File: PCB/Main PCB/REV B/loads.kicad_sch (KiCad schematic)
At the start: 13 parts, among them J10 Ignitor, J11 Auger, J12 FAN, K1 CPC1966Y, U7 AQH3223A, U8 AQH3223A

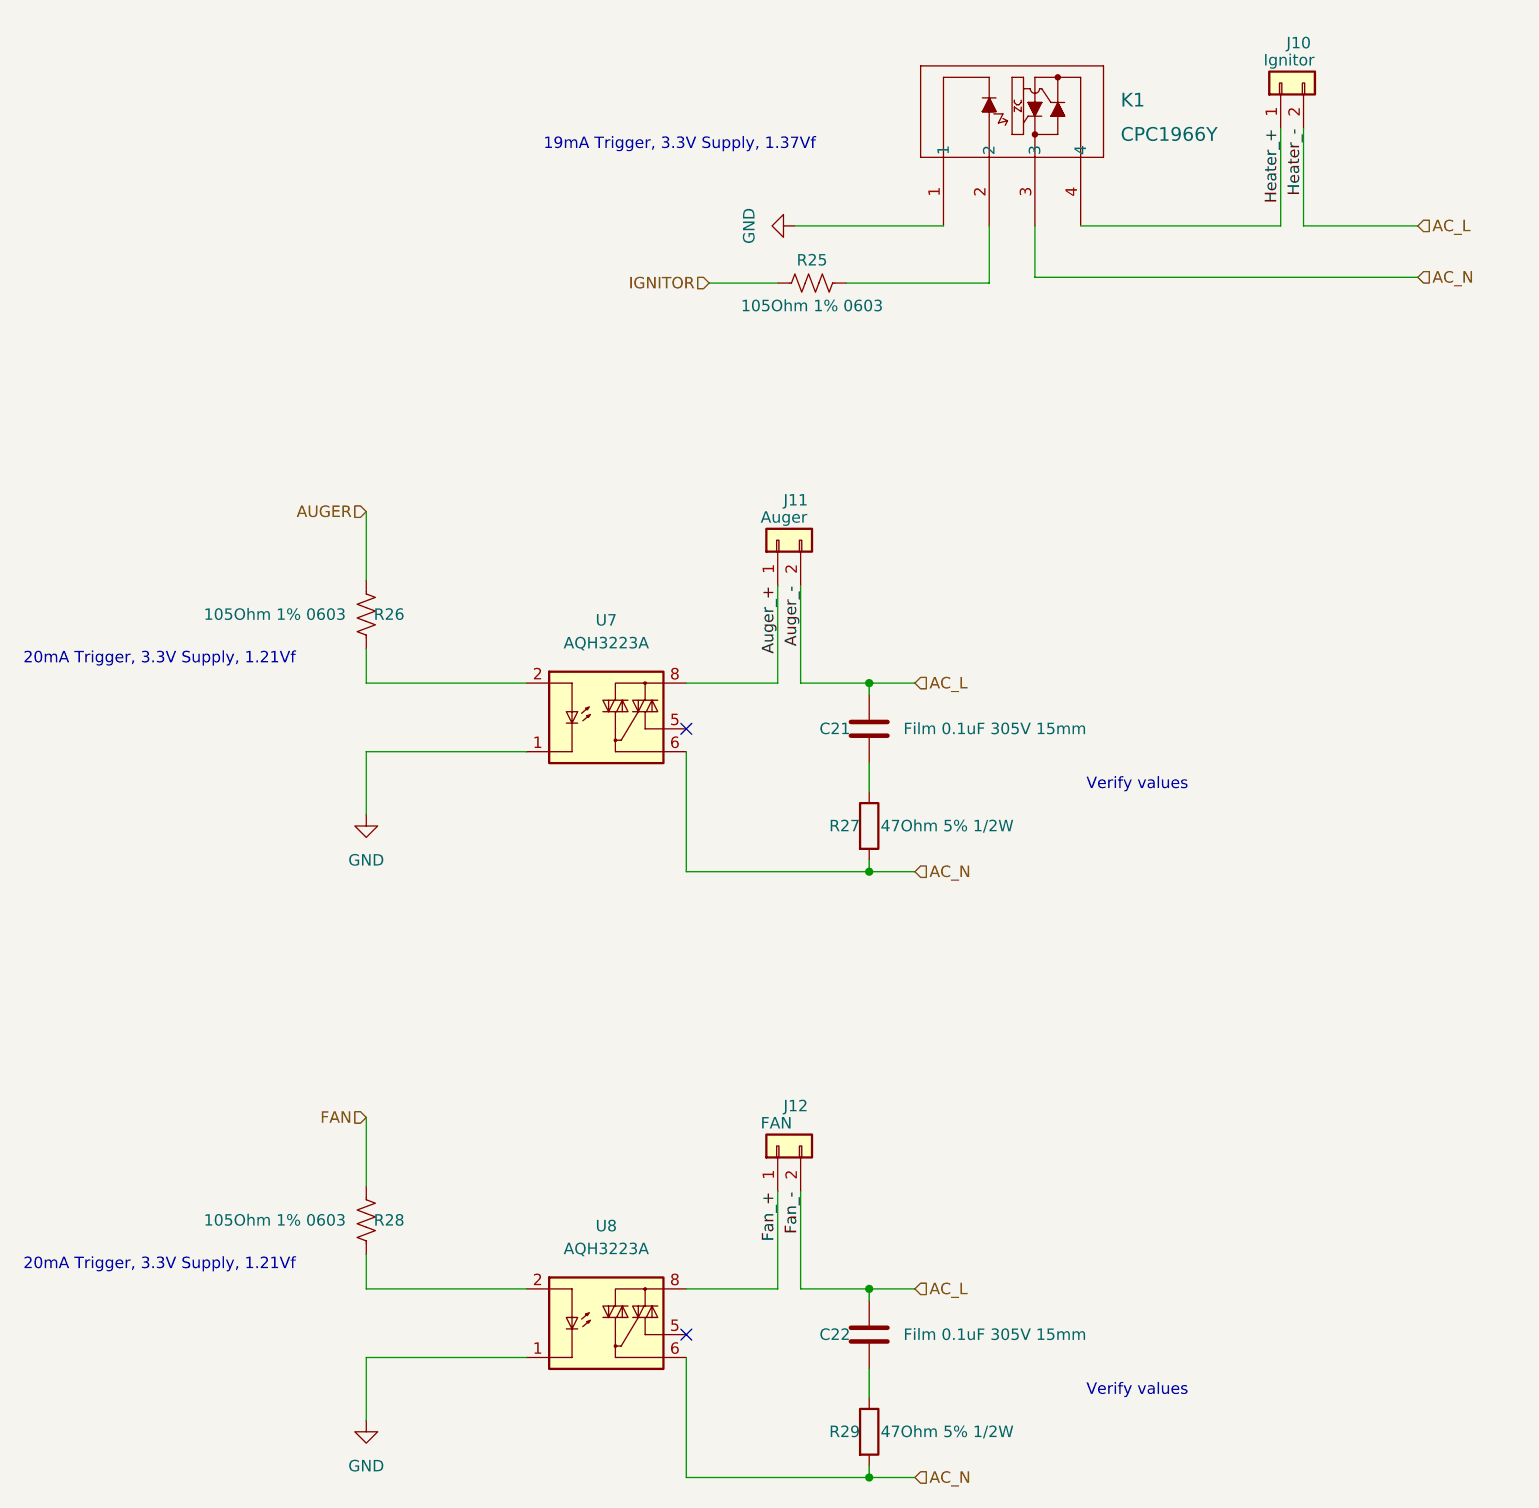
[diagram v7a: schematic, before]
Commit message: PCB schematic updates, added 5V power supply
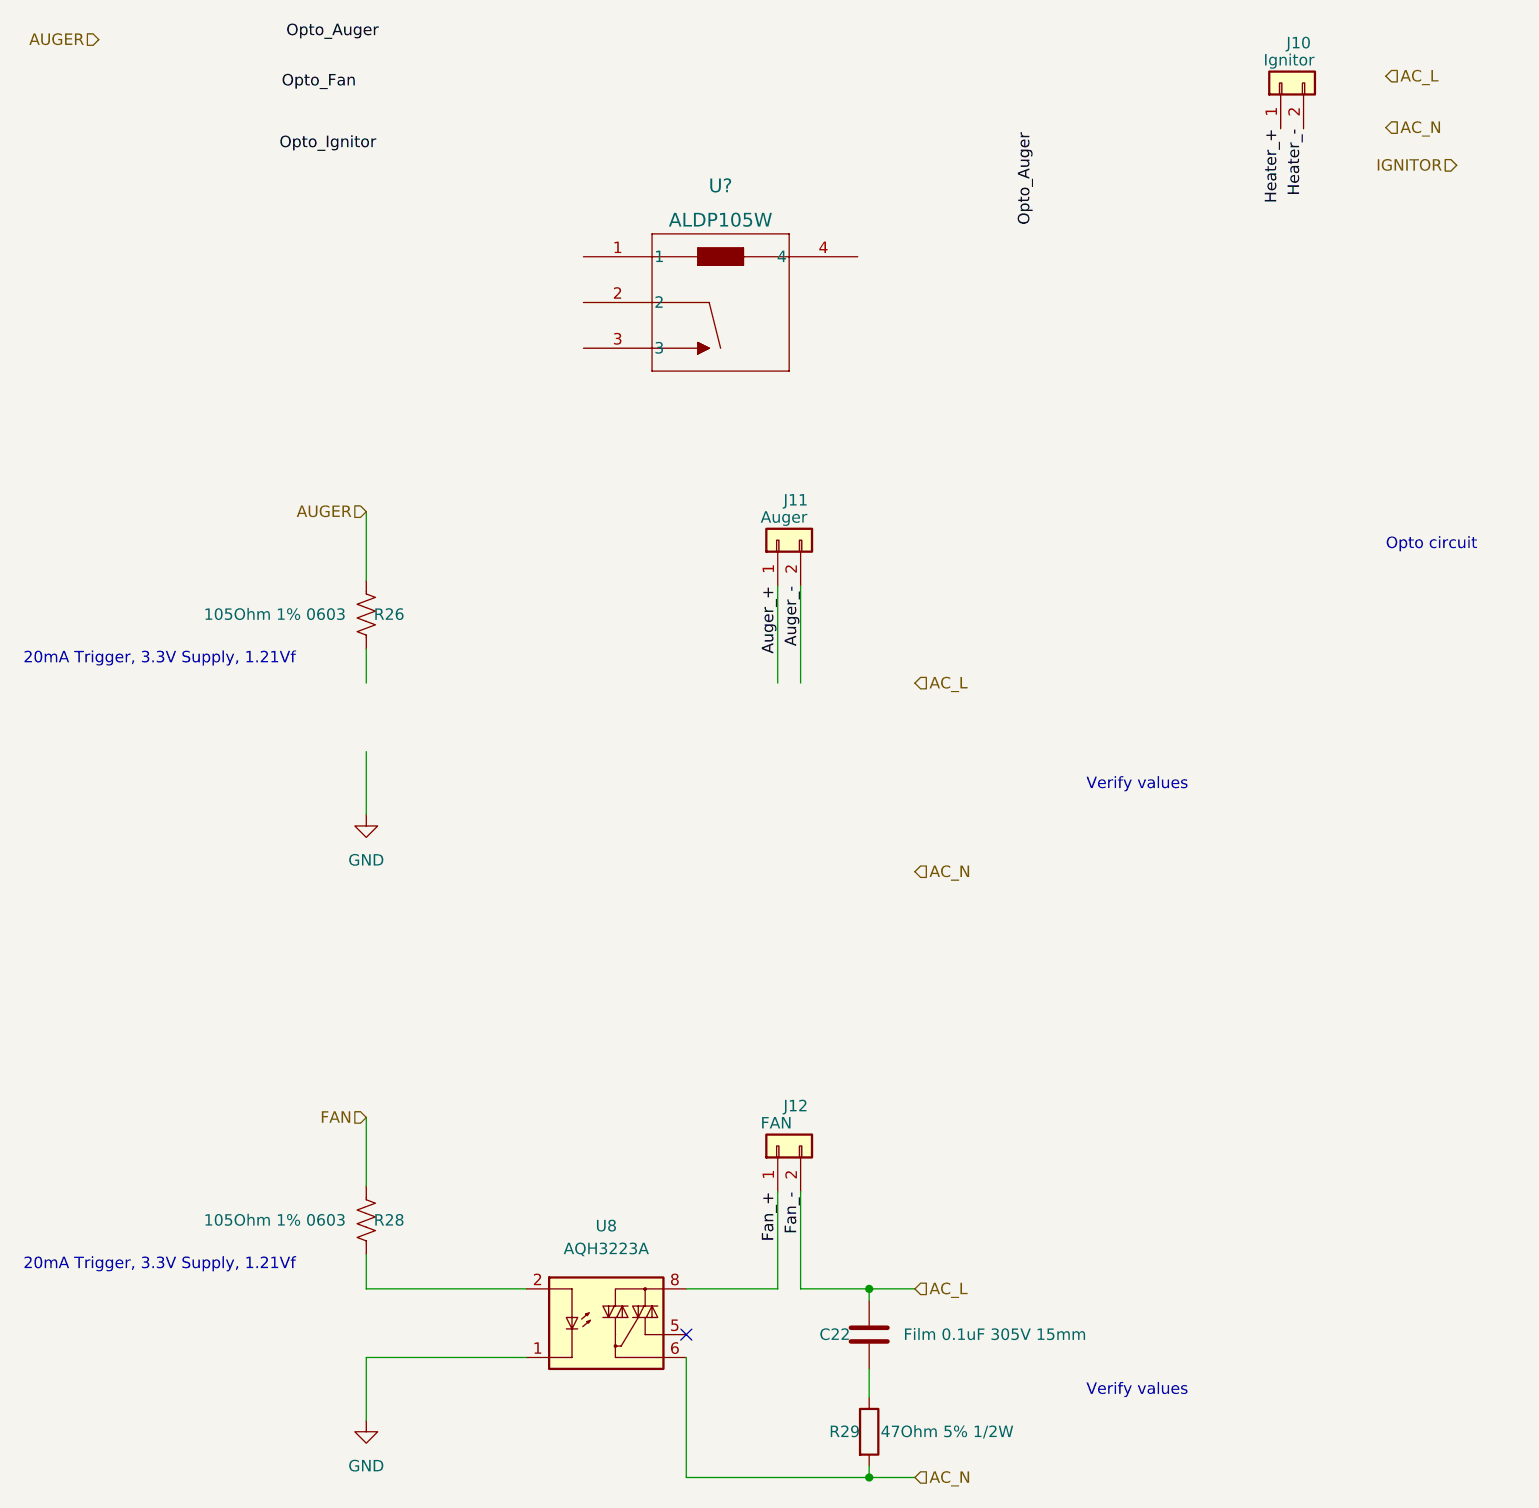
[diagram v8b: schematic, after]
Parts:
- removed C21: Film 0.1uF 305V 15mm, Capacitor_THT:C_Rect_L18.0mm_W6.0mm_P15.00mm_FKS3_FKP3, symbol Device:C
- removed K1: CPC1966Y, Customs Smoker:SIP4_CPC1966Y_LTF, symbol CPC1966Y:CPC1966Y
- removed R25: 105Ohm 1% 0603, Resistor_SMD:R_0603_1608Metric, symbol Device:R_US
- removed R27: 47Ohm 5% 1/2W, Resistor_THT:R_Axial_DIN0204_L3.6mm_D1.6mm_P5.08mm_Vertical, symbol Device:R
- removed U7: AQH3223A, Package_SO:SSO-7-8_6.4x9.78mm_P2.54mm, symbol Relay_SolidState:AQH3223A
- added U?: ALDP105W, PAN_ALD_PAN, symbol ALDP105W:ALDP105W
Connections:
- net AC_L: no longer J10.2 (Pin_2), J11.2 (Pin_2)
- new net Auger_-: J11.2 (Pin_2)
- new net Heater_-: J10.2 (Pin_2)
- no-connect marks 2 -> 1
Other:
- note added: "Opto circuit"
- note removed: "19mA Trigger, 3.3V Supply, 1.37Vf"
